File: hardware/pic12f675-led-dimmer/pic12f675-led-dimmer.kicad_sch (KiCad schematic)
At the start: 32 parts, among them Q1 Q_NPN, Q2 Q_NPN, Q3 Q_NPN, Q4 Q_NPN, Q5 Q_NPN, U1 PIC12F675-xP

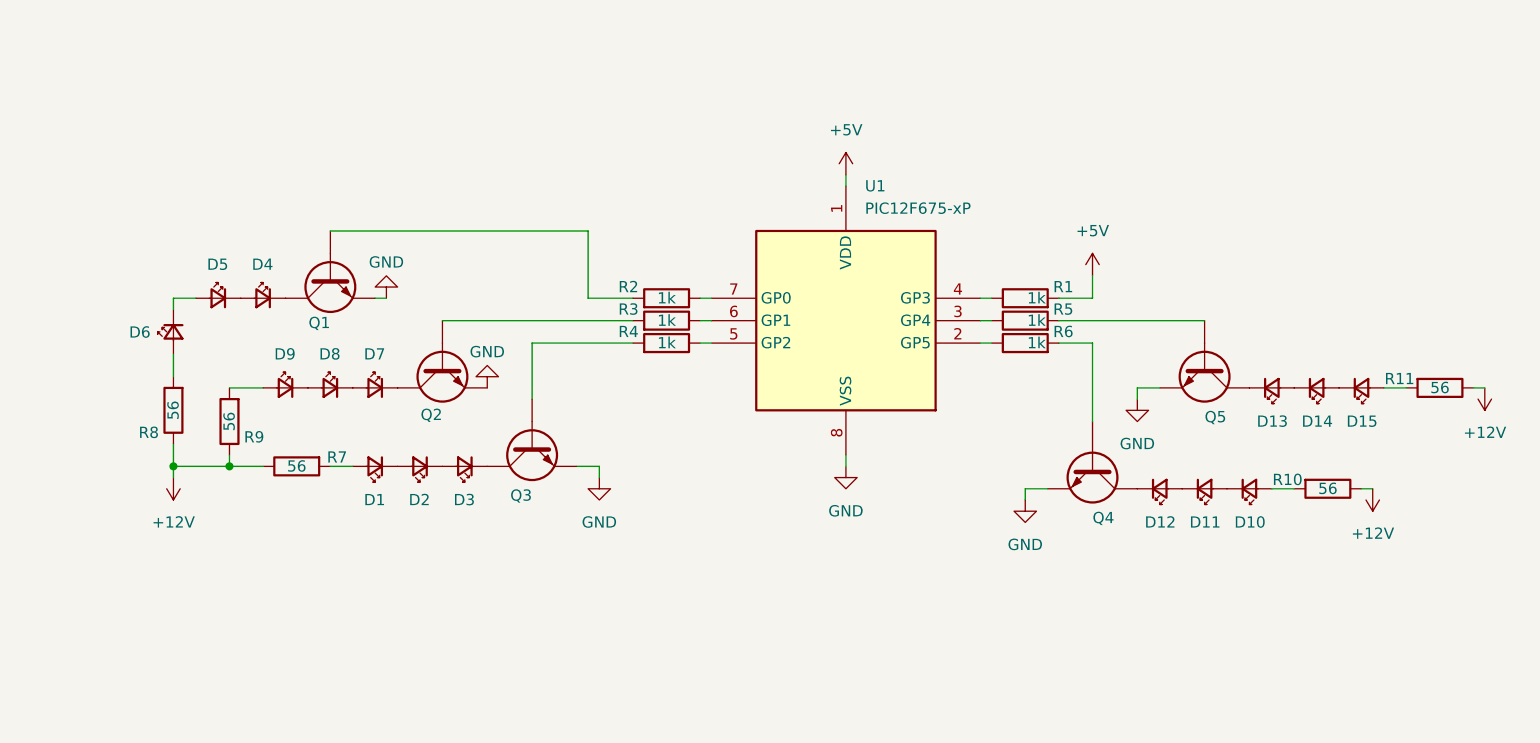
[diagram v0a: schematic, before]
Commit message: feat(hw): asignar huellas y definir layout preliminar de la PCB
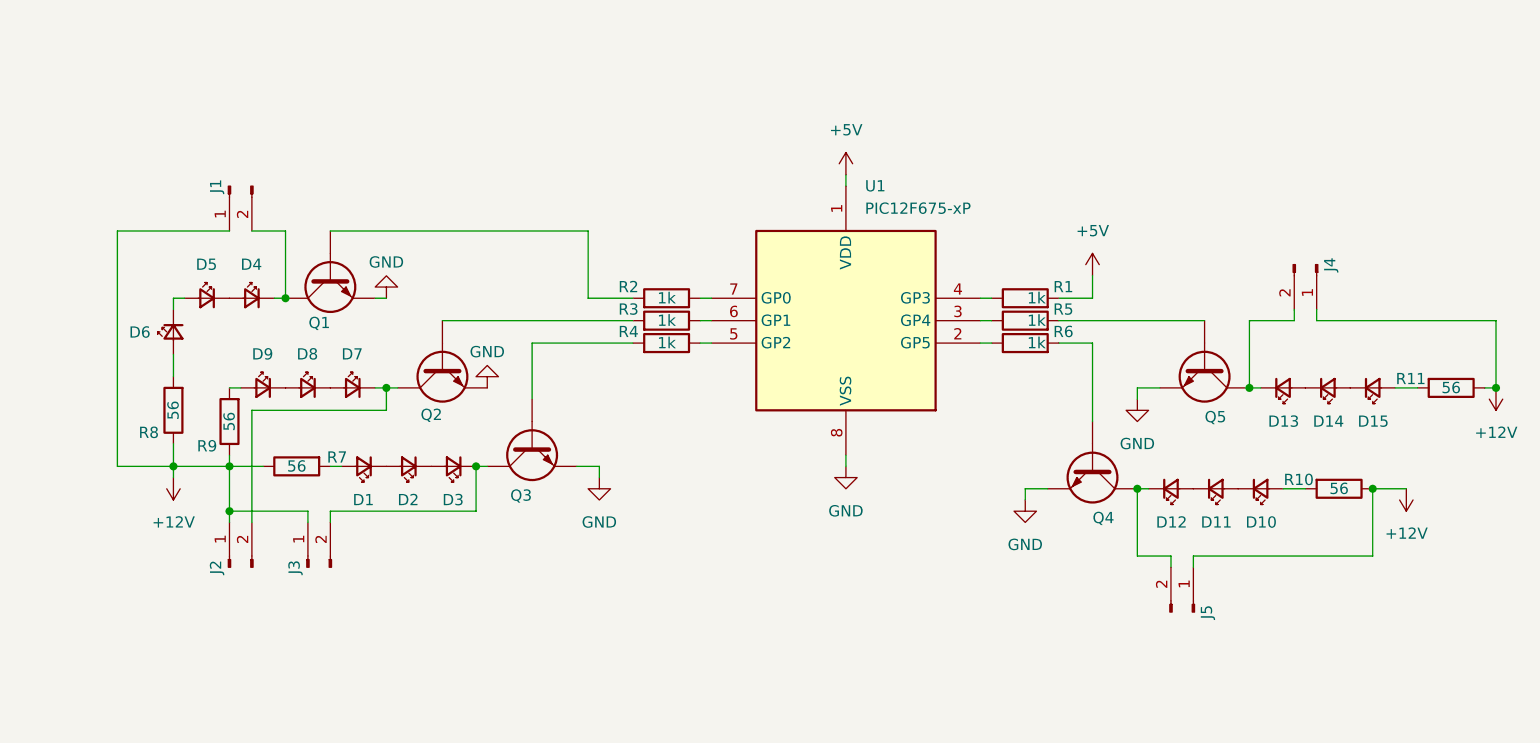
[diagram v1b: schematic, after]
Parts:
- added J1, J2, J3, J4, J5: Conn_01x02_Pin, Connector_JST:JST_XH_B2B-XH-A_1x02_P2.50mm_Vertical, symbol Connector:Conn_01x02_Pin
- D1, R1, R2, R3, R4, R5, R6: footprint (none) -> Resistor_THT:R_Axial_DIN0207_L6.3mm_D2.5mm_P10.16mm_Horizontal
- D10, D11, D12, D13, D14, D15: now left out of the parts list
- Q1, Q2, Q3, Q4, Q5: footprint (none) -> Package_TO_SOT_THT:TO-92_Inline
- R10, R11, R7, R8, R9: footprint (none) -> Resistor_THT:R_Axial_DIN0207_L6.3mm_D2.5mm_P10.16mm_Horizontal; now left out of the parts list
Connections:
- net +12V: now also J1.1 (Pin_1), J2.1 (Pin_1), J3.1 (Pin_1), J4.1 (Pin_1), J5.1 (Pin_1)
- net at D3.1 (K), Q3.C: now also J3.2 (Pin_2)
- net at D4.1 (K), Q1.C: now also J1.2 (Pin_2)
- net at D12.1 (K), Q4.C: now also J5.2 (Pin_2)
- net at D13.1 (K), Q5.C: now also J4.2 (Pin_2)
- net at D7.1 (K), Q2.C: now also J2.2 (Pin_2)
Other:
- moved on the sheet: D1, D10, D11, D12, D13, D14, D15, D2, D3, D4, D5, D7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

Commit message: refactor(hw): preparar espacio para integración de módulo buck step-down
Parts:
- added J6: Screw_Terminal_01x02, symbol Connector:Screw_Terminal_01x02
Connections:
- net +12V: now also J6.1 (Pin_1)
- net GND: now also J6.2 (Pin_2)
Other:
- moved on the sheet: D1, D10, D11, D12, D13, D14, D15, D2, D3, D4, D5, D6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
